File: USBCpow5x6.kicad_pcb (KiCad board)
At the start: 2 copper layers, 82.5 x 76.2 mm, 210 parts, among them CN1 CON_USB-C-6, J1 Conn_01x05, U1 LM1117-3.3

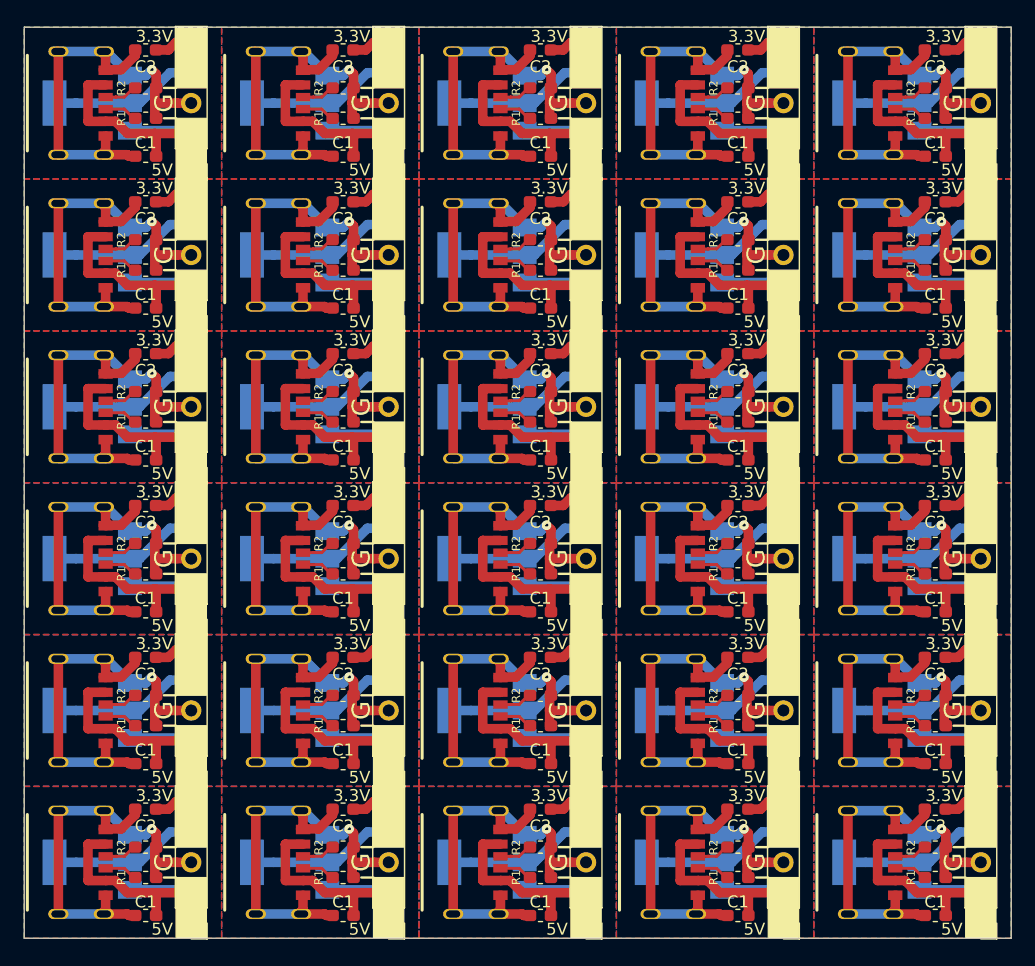
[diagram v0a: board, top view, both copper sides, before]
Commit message: 固定用ピンヘッダの穴を追加
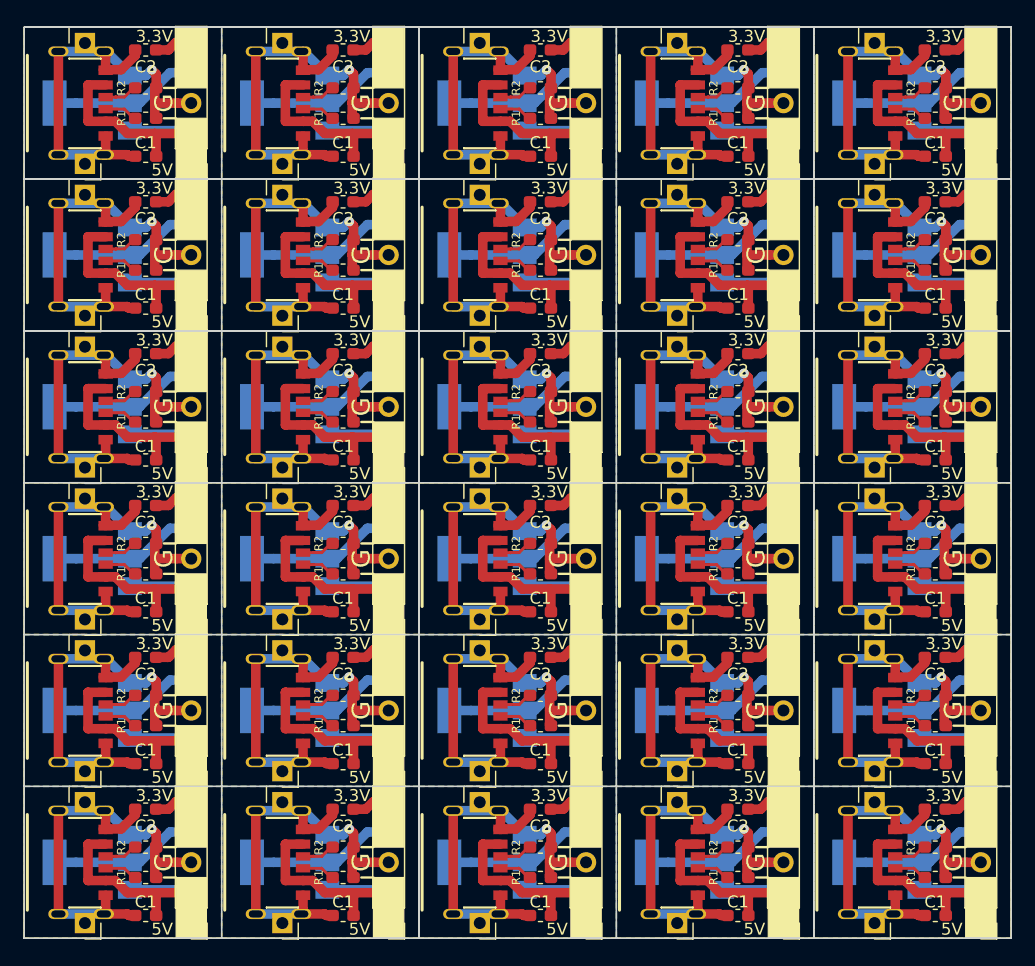
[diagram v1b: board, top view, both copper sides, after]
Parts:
- added J3: Conn_01x01, Connector_PinHeader_2.54mm:PinHeader_1x01_P2.54mm_Vertical, F.Cu at (71.1, 62.2)
- added J3: Conn_01x01, Connector_PinHeader_2.54mm:PinHeader_1x01_P2.54mm_Vertical, F.Cu at (5.08, 49.5)
- added J3: Conn_01x01, Connector_PinHeader_2.54mm:PinHeader_1x01_P2.54mm_Vertical, F.Cu at (71.1, 36.8)
- added J3: Conn_01x01, Connector_PinHeader_2.54mm:PinHeader_1x01_P2.54mm_Vertical, F.Cu at (54.6, 36.8)
- added J3: Conn_01x01, Connector_PinHeader_2.54mm:PinHeader_1x01_P2.54mm_Vertical, F.Cu at (38.1, 36.8)
- added J3: Conn_01x01, Connector_PinHeader_2.54mm:PinHeader_1x01_P2.54mm_Vertical, F.Cu at (21.6, 36.8)
- added J3: Conn_01x01, Connector_PinHeader_2.54mm:PinHeader_1x01_P2.54mm_Vertical, F.Cu at (5.08, 36.8)
- added J3: Conn_01x01, Connector_PinHeader_2.54mm:PinHeader_1x01_P2.54mm_Vertical, F.Cu at (71.1, 24.1)
- added J3: Conn_01x01, Connector_PinHeader_2.54mm:PinHeader_1x01_P2.54mm_Vertical, F.Cu at (54.6, 24.1)
- added J3: Conn_01x01, Connector_PinHeader_2.54mm:PinHeader_1x01_P2.54mm_Vertical, F.Cu at (38.1, 24.1)
- added J3: Conn_01x01, Connector_PinHeader_2.54mm:PinHeader_1x01_P2.54mm_Vertical, F.Cu at (21.6, 24.1)
- added J3: Conn_01x01, Connector_PinHeader_2.54mm:PinHeader_1x01_P2.54mm_Vertical, F.Cu at (54.6, 62.2)
- added J3: Conn_01x01, Connector_PinHeader_2.54mm:PinHeader_1x01_P2.54mm_Vertical, F.Cu at (5.08, 24.1)
- added J3: Conn_01x01, Connector_PinHeader_2.54mm:PinHeader_1x01_P2.54mm_Vertical, F.Cu at (71.1, 11.4)
- added J3: Conn_01x01, Connector_PinHeader_2.54mm:PinHeader_1x01_P2.54mm_Vertical, F.Cu at (54.6, 11.4)
- added J3: Conn_01x01, Connector_PinHeader_2.54mm:PinHeader_1x01_P2.54mm_Vertical, F.Cu at (38.1, 11.4)
- added J3: Conn_01x01, Connector_PinHeader_2.54mm:PinHeader_1x01_P2.54mm_Vertical, F.Cu at (21.6, 11.4)
- added J3: Conn_01x01, Connector_PinHeader_2.54mm:PinHeader_1x01_P2.54mm_Vertical, F.Cu at (5.08, 11.4)
- added J3: Conn_01x01, Connector_PinHeader_2.54mm:PinHeader_1x01_P2.54mm_Vertical, F.Cu at (71.1, -1.27)
- added J3: Conn_01x01, Connector_PinHeader_2.54mm:PinHeader_1x01_P2.54mm_Vertical, F.Cu at (54.6, -1.27)
- added J3: Conn_01x01, Connector_PinHeader_2.54mm:PinHeader_1x01_P2.54mm_Vertical, F.Cu at (38.1, -1.27)
- added J3: Conn_01x01, Connector_PinHeader_2.54mm:PinHeader_1x01_P2.54mm_Vertical, F.Cu at (21.6, -1.27)
- added J3: Conn_01x01, Connector_PinHeader_2.54mm:PinHeader_1x01_P2.54mm_Vertical, F.Cu at (38.1, 62.2)
- added J3: Conn_01x01, Connector_PinHeader_2.54mm:PinHeader_1x01_P2.54mm_Vertical, F.Cu at (5.08, -1.27)
- added J3: Conn_01x01, Connector_PinHeader_2.54mm:PinHeader_1x01_P2.54mm_Vertical, F.Cu at (21.6, 62.2)
- added J3: Conn_01x01, Connector_PinHeader_2.54mm:PinHeader_1x01_P2.54mm_Vertical, F.Cu at (5.08, 62.2)
- added J3: Conn_01x01, Connector_PinHeader_2.54mm:PinHeader_1x01_P2.54mm_Vertical, F.Cu at (71.1, 49.5)
- added J3: Conn_01x01, Connector_PinHeader_2.54mm:PinHeader_1x01_P2.54mm_Vertical, F.Cu at (54.6, 49.5)
- added J3: Conn_01x01, Connector_PinHeader_2.54mm:PinHeader_1x01_P2.54mm_Vertical, F.Cu at (38.1, 49.5)
- added J3: Conn_01x01, Connector_PinHeader_2.54mm:PinHeader_1x01_P2.54mm_Vertical, F.Cu at (21.6, 49.5)
- added Jq: Conn_01x01, Connector_PinHeader_2.54mm:PinHeader_1x01_P2.54mm_Vertical, F.Cu at (71.1, 52.1)
- added Jq: Conn_01x01, Connector_PinHeader_2.54mm:PinHeader_1x01_P2.54mm_Vertical, F.Cu at (5.08, 39.4)
- added Jq: Conn_01x01, Connector_PinHeader_2.54mm:PinHeader_1x01_P2.54mm_Vertical, F.Cu at (71.1, 26.7)
- added Jq: Conn_01x01, Connector_PinHeader_2.54mm:PinHeader_1x01_P2.54mm_Vertical, F.Cu at (54.6, 26.7)
- added Jq: Conn_01x01, Connector_PinHeader_2.54mm:PinHeader_1x01_P2.54mm_Vertical, F.Cu at (38.1, 26.7)
- added Jq: Conn_01x01, Connector_PinHeader_2.54mm:PinHeader_1x01_P2.54mm_Vertical, F.Cu at (21.6, 26.7)
- added Jq: Conn_01x01, Connector_PinHeader_2.54mm:PinHeader_1x01_P2.54mm_Vertical, F.Cu at (5.08, 26.7)
- added Jq: Conn_01x01, Connector_PinHeader_2.54mm:PinHeader_1x01_P2.54mm_Vertical, F.Cu at (71.1, 14.0)
- added Jq: Conn_01x01, Connector_PinHeader_2.54mm:PinHeader_1x01_P2.54mm_Vertical, F.Cu at (54.6, 14.0)
- added Jq: Conn_01x01, Connector_PinHeader_2.54mm:PinHeader_1x01_P2.54mm_Vertical, F.Cu at (38.1, 14.0)
- added Jq: Conn_01x01, Connector_PinHeader_2.54mm:PinHeader_1x01_P2.54mm_Vertical, F.Cu at (21.6, 14.0)
- added Jq: Conn_01x01, Connector_PinHeader_2.54mm:PinHeader_1x01_P2.54mm_Vertical, F.Cu at (54.6, 52.1)
- added Jq: Conn_01x01, Connector_PinHeader_2.54mm:PinHeader_1x01_P2.54mm_Vertical, F.Cu at (5.08, 14.0)
- added Jq: Conn_01x01, Connector_PinHeader_2.54mm:PinHeader_1x01_P2.54mm_Vertical, F.Cu at (71.1, 1.33)
- added Jq: Conn_01x01, Connector_PinHeader_2.54mm:PinHeader_1x01_P2.54mm_Vertical, F.Cu at (54.6, 1.33)
- added Jq: Conn_01x01, Connector_PinHeader_2.54mm:PinHeader_1x01_P2.54mm_Vertical, F.Cu at (38.1, 1.33)
- added Jq: Conn_01x01, Connector_PinHeader_2.54mm:PinHeader_1x01_P2.54mm_Vertical, F.Cu at (21.6, 1.33)
- added Jq: Conn_01x01, Connector_PinHeader_2.54mm:PinHeader_1x01_P2.54mm_Vertical, F.Cu at (5.08, 1.33)
- added Jq: Conn_01x01, Connector_PinHeader_2.54mm:PinHeader_1x01_P2.54mm_Vertical, F.Cu at (71.1, -11.4)
- added Jq: Conn_01x01, Connector_PinHeader_2.54mm:PinHeader_1x01_P2.54mm_Vertical, F.Cu at (54.6, -11.4)
- added Jq: Conn_01x01, Connector_PinHeader_2.54mm:PinHeader_1x01_P2.54mm_Vertical, F.Cu at (38.1, -11.4)
- added Jq: Conn_01x01, Connector_PinHeader_2.54mm:PinHeader_1x01_P2.54mm_Vertical, F.Cu at (21.6, -11.4)
- added Jq: Conn_01x01, Connector_PinHeader_2.54mm:PinHeader_1x01_P2.54mm_Vertical, F.Cu at (38.1, 52.1)
- added Jq: Conn_01x01, Connector_PinHeader_2.54mm:PinHeader_1x01_P2.54mm_Vertical, F.Cu at (5.08, -11.4)
- added Jq: Conn_01x01, Connector_PinHeader_2.54mm:PinHeader_1x01_P2.54mm_Vertical, F.Cu at (21.6, 52.1)
- added Jq: Conn_01x01, Connector_PinHeader_2.54mm:PinHeader_1x01_P2.54mm_Vertical, F.Cu at (5.08, 52.1)
- added Jq: Conn_01x01, Connector_PinHeader_2.54mm:PinHeader_1x01_P2.54mm_Vertical, F.Cu at (71.1, 39.4)
- added Jq: Conn_01x01, Connector_PinHeader_2.54mm:PinHeader_1x01_P2.54mm_Vertical, F.Cu at (54.6, 39.4)
- added Jq: Conn_01x01, Connector_PinHeader_2.54mm:PinHeader_1x01_P2.54mm_Vertical, F.Cu at (38.1, 39.4)
- added Jq: Conn_01x01, Connector_PinHeader_2.54mm:PinHeader_1x01_P2.54mm_Vertical, F.Cu at (21.6, 39.4)
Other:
- outline, holes or cut-outs redrawn
